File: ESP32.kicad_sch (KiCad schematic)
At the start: 24 parts, among them IC1 LY68L6400SLIT, Q3 MUN5211DW1, U10 ESP32-S2FH4, U11 W25Q128JVS, U8 CP2104, Y4 40MHz

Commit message: тестирование
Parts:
- removed F2, F3: BLM15BC241SN1D, Fuse:Fuse_0402_1005Metric, symbol Device:Fuse
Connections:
- net ESP_3V3: now also U10.1 (VDDA@0), U10.20 (VDD3P3_RTC), U10.27 (VDD3P3_RTC_IO), U10.3 (VDD3P3@0), U10.4 (VDD3P3@1), U10.45 (VDD3P3_CPU), U10.51 (VDDA@1), U10.54 (VDDA@2)
- no-connect marks 41 -> 43
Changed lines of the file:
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@@
 (kicad_sch (version 20211123) (generator eeschema)
   (paper "A3")
-  (junction (at 107.95 22.86) (diameter 0) (color 0 0 0 0)
+  (junction (at 223.52 52.07) (diameter 0) (color 0 0 0 0)
+  )
+  (junction (at 60.96 152.4) (diameter 0) (color 0 0 0 0)
+  )
+  (junction (at 39.37 62.23) (diameter 0) (color 0 0 0 0)
+  )
+  (junction (at 218.44 46.99) (diameter 0) (color 0 0 0 0)
+  )
+  (junction (at 97.79 203.2) (diameter 0) (color 0 0 0 0)
+  )
+  (junction (at 25.4 69.85) (diameter 0) (color 0 0 0 0)
+  )
+  (junction (at 102.87 34.29) (diameter 0) (color 0 0 0 0)
+  )
+  (junction (at 30.48 69.85) (diameter 0) (color 0 0 0 0)
+  )
+  (junction (at 223.52 96.52) (diameter 0) (color 0 0 0 0)
+  )
+  (junction (at 130.81 195.58) (diameter 0) (color 0 0 0 0)
+  )
+  (junction (at 127 30.48) (diameter 0) (color 0 0 0 0)
+  )
+  (junction (at 138.43 22.86) (diameter 0) (color 0 0 0 0)
+  )
+  (junction (at 127 22.86) (diameter 0) (color 0 0 0 0)
   )
   (junction (at 92.71 34.29) (diameter 0) (color 0 0 0 0)
   )
-  (junction (at 223.52 52.07) (diameter 0) (color 0 0 0 0)
-  )
-  (junction (at 60.96 152.4) (diameter 0) (color 0 0 0 0)
-  )
-  (junction (at 39.37 62.23) (diameter 0) (color 0 0 0 0)
-  )
-  (junction (at 218.44 46.99) (diameter 0) (color 0 0 0 0)
-  )
-  (junction (at 97.79 203.2) (diameter 0) (color 0 0 0 0)
-  )
-  (junction (at 87.63 34.29) (diameter 0) (color 0 0 0 0)
-  )
-  (junction (at 25.4 69.85) (diameter 0) (color 0 0 0 0)
-  )
-  (junction (at 102.87 34.29) (diameter 0) (color 0 0 0 0)
-  )
-  (junction (at 30.48 69.85) (diameter 0) (color 0 0 0 0)
-  )
-  (junction (at 223.52 96.52) (diameter 0) (color 0 0 0 0)
-  )
-  (junction (at 130.81 195.58) (diameter 0) (color 0 0 0 0)
-  )
-  (junction (at 127 30.48) (diameter 0) (color 0 0 0 0)
-  )
-  (junction (at 138.43 22.86) (diameter 0) (color 0 0 0 0)
-  )
-  (junction (at 127 22.86) (diameter 0) (color 0 0 0 0)
-  )
   (junction (at 97.79 34.29) (diameter 0) (color 0 0 0 0)
   )
@@
   (junction (at 149.86 22.86) (diameter 0) (color 0 0 0 0)
   )
+  (junction (at 105.41 34.29) (diameter 0) (color 0 0 0 0)
+  )
   (junction (at 138.43 30.48) (diameter 0) (color 0 0 0 0)
   )
@@
   )
   (junction (at 21.59 62.23) (diameter 0) (color 0 0 0 0)
+  )
+  (junction (at 90.17 34.29) (diameter 0) (color 0 0 0 0)
   )
   (junction (at 220.98 90.17) (diameter 0) (color 0 0 0 0)
@@
   (no_connect (at 73.66 172.72))
   (no_connect (at 73.66 175.26))
+  (no_connect (at 66.04 48.26))
+  (no_connect (at 66.04 45.72))
   (bus_entry (at 148.59 68.58) (size -2.54 2.54)
     (stroke (width 0) (type default) (color 0 0 0 0))
@@
     (stroke (width 0) (type default) (color 0 0 0 0))
   )
+  (wire (pts (xy 105.41 22.86) (xy 105.41 34.29))
+    (stroke (width 0) (type default) (color 0 0 0 0))
+  )
   (polyline (pts (xy 199.39 12.7) (xy 199.39 130.81))
     (stroke (width 0) (type default) (color 0 0 0 0))
@@
     (stroke (width 0) (type default) (color 0 0 0 0))
   )
-  (wire (pts (xy 93.98 30.48) (xy 92.71 30.48))
-    (stroke (width 0) (type default) (color 0 0 0 0))
-  )
   (wire (pts (xy 138.43 22.86) (xy 127 22.86))
     (stroke (width 0) (type default) (color 0 0 0 0))
@@
     (stroke (width 0) (type default) (color 0 0 0 0))
   )
-  (wire (pts (xy 101.6 30.48) (xy 107.95 30.48))
-    (stroke (width 0) (type default) (color 0 0 0 0))
-  )
   (wire (pts (xy 46.99 152.4) (xy 58.42 152.4))
     (stroke (width 0) (type default) (color 0 0 0 0))
@@
     (stroke (width 0) (type default) (color 0 0 0 0))
   )
+  (wire (pts (xy 90.17 34.29) (xy 92.71 34.29))
+    (stroke (width 0) (type default) (color 0 0 0 0))
+  )
   (polyline (pts (xy 12.7 132.08) (xy 147.32 132.08))
     (stroke (width 0) (type default) (color 0 0 0 0))
@@
     (stroke (width 0) (type default) (color 0 0 0 0))
   )
-  (wire (pts (xy 107.95 22.86) (xy 101.6 22.86))
-    (stroke (width 0) (type default) (color 0 0 0 0))
-  )
   (wire (pts (xy 130.81 195.58) (xy 130.81 194.31))
     (stroke (width 0) (type default) (color 0 0 0 0))
@@
     (stroke (width 0) (type default) (color 0 0 0 0))
   )
-  (wire (pts (xy 115.57 22.86) (xy 107.95 22.86))
-    (stroke (width 0) (type default) (color 0 0 0 0))
-  )
   (wire (pts (xy 163.83 46.99) (xy 165.1 46.99))
     (stroke (width 0) (type default) (color 0 0 0 0))
@@
     (stroke (width 0) (type default) (color 0 0 0 0))
   )
-  (wire (pts (xy 92.71 34.29) (xy 92.71 30.48))
-    (stroke (width 0) (type default) (color 0 0 0 0))
-  )
   (wire (pts (xy 130.81 185.42) (xy 130.81 186.69))
     (stroke (width 0) (type default) (color 0 0 0 0))
@@
     (stroke (width 0) (type default) (color 0 0 0 0))
   )
-  (wire (pts (xy 87.63 22.86) (xy 93.98 22.86))
-    (stroke (width 0) (type default) (color 0 0 0 0))
-  )
   (polyline (pts (xy 147.32 229.87) (xy 12.7 229.87))
     (stroke (width 0) (type default) (color 0 0 0 0))
@@
     (stroke (width 0) (type default) (color 0 0 0 0))
   )
-  (wire (pts (xy 87.63 34.29) (xy 87.63 22.86))
-    (stroke (width 0) (type default) (color 0 0 0 0))
-  )
   (wire (pts (xy 115.57 30.48) (xy 127 30.48))
     (stroke (width 0) (type default) (color 0 0 0 0))
@@
     (stroke (width 0) (type default) (color 0 0 0 0))
   )
-  (wire (pts (xy 107.95 30.48) (xy 107.95 22.86))
-    (stroke (width 0) (type default) (color 0 0 0 0))
-  )
   (wire (pts (xy 110.49 195.58) (xy 130.81 195.58))
     (stroke (width 0) (type default) (color 0 0 0 0))
@@
   )
   (wire (pts (xy 110.49 214.63) (xy 110.49 212.09))
+    (stroke (width 0) (type default) (color 0 0 0 0))
+  )
+  (wire (pts (xy 105.41 22.86) (xy 115.57 22.86))
     (stroke (width 0) (type default) (color 0 0 0 0))
   )
@@
     (pin "2")
   )
-  (symbol (lib_id "Device:Fuse") (at 97.79 22.86 270) (unit 1)
-    (in_bom yes) (on_board yes)
-    (property "Reference" "F2" (id 0) (at 97.79 17.8562 90))
-    (property "Value" "BLM15BC241SN1D" (id 1) (at 97.79 20.32 90))
-    (property "Footprint" "Fuse:Fuse_0402_1005Metric" (id 2) (at 97.79 21.082 90)
-      (effects (font (size 1.27 1.27)) hide)
-    )
-    (property "Datasheet" "~" (id 3) (at 97.79 22.86 0)
-      (effects (font (size 1.27 1.27)) hide)
-    )
-    (property "Manufacturer_Part_Number" "BLM15BC241SN1D" (id 8) (at 97.79 22.86 0)
-      (effects (font (size 1.27 1.27)) hide)
-    )
-    (pin "1")
-    (pin "2")
-  )
   (symbol (lib_id "Device:C") (at 115.57 26.67 0) (unit 1)
     (in_bom yes) (on_board yes)
@@
       (effects (font (size 1.27 1.27)) hide)
     )
-    (pin "1")
-    (pin "2")
-  )
-  (symbol (lib_id "Device:Fuse") (at 97.79 30.48 270) (unit 1)
-    (in_bom yes) (on_board yes)
-    (property "Reference" "F3" (id 0) (at 97.79 25.4762 90))
-    (property "Value" "BLM15BC241SN1D" (id 1) (at 97.79 27.94 90))
-    (property "Footprint" "Fuse:Fuse_0402_1005Metric" (id 2) (at 97.79 28.702 90)
-      (effects (font (size 1.27 1.27)) hide)
-    )
-    (property "Datasheet" "~" (id 3) (at 97.79 30.48 0)
-      (effects (font (size 1.27 1.27)) hide)
-    )
-    (property "Manufacturer_Part_Number" "BLM15BC241SN1D" (id 8) (at 97.79 30.48 0)
-      (effects (font (size 1.27 1.27)) hide)
-    )

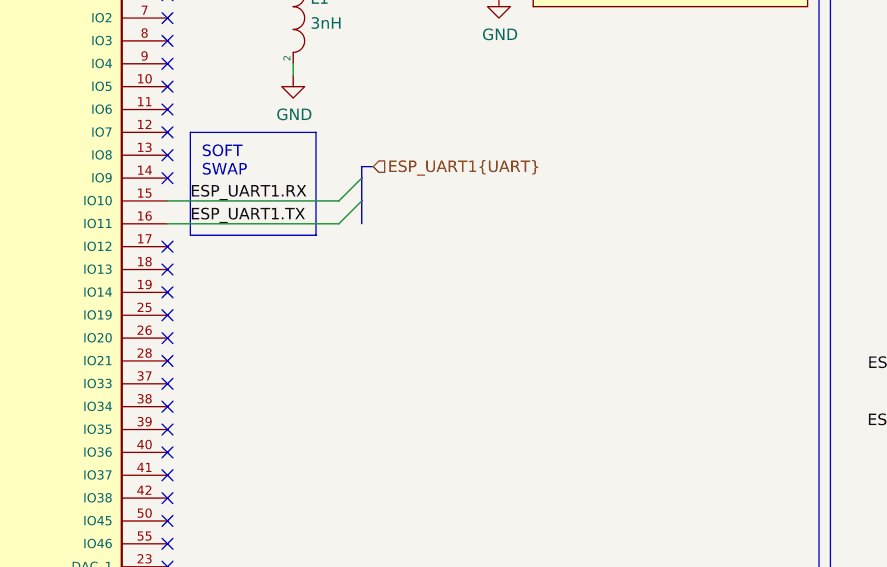
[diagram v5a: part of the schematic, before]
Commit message: Adding esp32 gpio pins
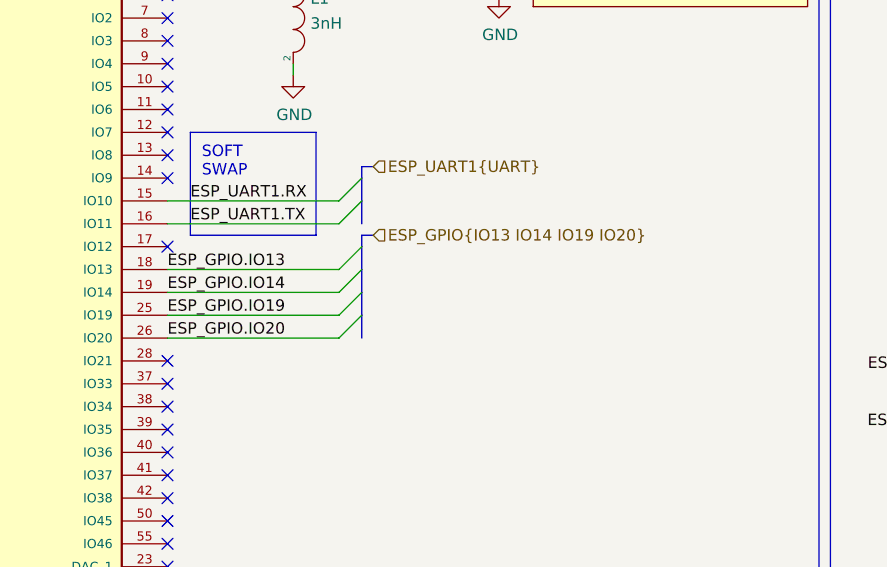
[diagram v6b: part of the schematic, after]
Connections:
- net ESP_GPIO.IO13: now reaches U10.18 (IO13)
- net ESP_GPIO.IO14: now reaches U10.19 (IO14)
- net ESP_GPIO.IO19: now reaches U10.25 (IO19)
- net ESP_GPIO.IO20: now reaches U10.26 (IO20)
- no-connect marks 43 -> 39
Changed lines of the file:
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@@
   (no_connect (at 127 55.88))
   (no_connect (at 127 58.42))
-  (no_connect (at 127 86.36))
-  (no_connect (at 127 83.82))
-  (no_connect (at 127 81.28))
-  (no_connect (at 127 78.74))
   (no_connect (at 127 76.2))
   (no_connect (at 127 66.04))
@@
   (no_connect (at 66.04 48.26))
   (no_connect (at 66.04 45.72))
+  (bus_entry (at 148.59 76.2) (size -2.54 2.54)
+    (stroke (width 0) (type default) (color 0 0 0 0))
+  )
+  (bus_entry (at 148.59 78.74) (size -2.54 2.54)
+    (stroke (width 0) (type default) (color 0 0 0 0))
+  )
   (bus_entry (at 148.59 68.58) (size -2.54 2.54)
     (stroke (width 0) (type default) (color 0 0 0 0))
@@
     (stroke (width 0) (type default) (color 0 0 0 0))
   )
+  (bus_entry (at 148.59 83.82) (size -2.54 2.54)
+    (stroke (width 0) (type default) (color 0 0 0 0))
+  )
   (bus_entry (at 31.75 170.18) (size 2.54 2.54)
     (stroke (width 0) (type default) (color 0 0 0 0))
@@
     (stroke (width 0) (type default) (color 0 0 0 0))
   )
+  (bus_entry (at 148.59 81.28) (size -2.54 2.54)
+    (stroke (width 0) (type default) (color 0 0 0 0))
+  )
   (bus (pts (xy 148.59 71.12) (xy 148.59 68.58))
     (stroke (width 0) (type default) (color 0 0 0 0))
@@
     (stroke (width 0) (type default) (color 0 0 0 0))
   )
+  (bus (pts (xy 148.59 76.2) (xy 148.59 74.93))
+    (stroke (width 0) (type default) (color 0 0 0 0))
+  )
   (wire (pts (xy 138.43 22.86) (xy 127 22.86))
     (stroke (width 0) (type default) (color 0 0 0 0))
@@
     (stroke (width 0) (type default) (color 0 0 0 0))
   )
+  (bus (pts (xy 148.59 76.2) (xy 148.59 78.74))
+    (stroke (width 0) (type default) (color 0 0 0 0))
+  )
   (wire (pts (xy 63.5 66.04) (xy 66.04 66.04))
     (stroke (width 0) (type default) (color 0 0 0 0))
@@
     (stroke (width 0) (type default) (color 0 0 0 0))
   )
+  (wire (pts (xy 127 83.82) (xy 146.05 83.82))
+    (stroke (width 0) (type default) (color 0 0 0 0))
+  )
   (wire (pts (xy 110.49 208.28) (xy 110.49 210.82))
     (stroke (width 0) (type default) (color 0 0 0 0))
@@
     (stroke (width 0) (type default) (color 0 0 0 0))
   )
+  (wire (pts (xy 127 81.28) (xy 146.05 81.28))
+    (stroke (width 0) (type default) (color 0 0 0 0))
+  )
   (wire (pts (xy 99.06 210.82) (xy 99.06 219.71))
     (stroke (width 0) (type default) (color 0 0 0 0))
@@
     (stroke (width 0) (type default) (color 0 0 0 0))
   )
+  (bus (pts (xy 148.59 74.93) (xy 149.86 74.93))
+    (stroke (width 0) (type default) (color 0 0 0 0))
+  )
   (wire (pts (xy 130.81 185.42) (xy 130.81 186.69))
     (stroke (width 0) (type default) (color 0 0 0 0))
@@
     (stroke (width 0) (type default) (color 0 0 0 0))
   )
+  (bus (pts (xy 148.59 78.74) (xy 148.59 81.28))
+    (stroke (width 0) (type default) (color 0 0 0 0))
+  )
   (wire (pts (xy 127 71.12) (xy 146.05 71.12))
     (stroke (width 0) (type default) (color 0 0 0 0))
@@
     (stroke (width 0) (type default) (color 0 0 0 0))
   )
+  (bus (pts (xy 148.59 83.82) (xy 148.59 86.36))
+    (stroke (width 0) (type default) (color 0 0 0 0))
+  )
   (wire (pts (xy 127 30.48) (xy 138.43 30.48))
     (stroke (width 0) (type default) (color 0 0 0 0))
@@
     (stroke (width 0) (type default) (color 0 0 0 0))
   )
+  (wire (pts (xy 127 86.36) (xy 146.05 86.36))
+    (stroke (width 0) (type default) (color 0 0 0 0))
+  )
   (wire (pts (xy 257.81 44.45) (xy 252.73 44.45))
     (stroke (width 0) (type default) (color 0 0 0 0))
@@
     (stroke (width 0) (type default) (color 0 0 0 0))
   )
+  (bus (pts (xy 148.59 81.28) (xy 148.59 83.82))
+    (stroke (width 0) (type default) (color 0 0 0 0))
+  )
   (wire (pts (xy 115.57 30.48) (xy 127 30.48))
     (stroke (width 0) (type default) (color 0 0 0 0))
@@
   )
   (wire (pts (xy 130.81 196.85) (xy 130.81 195.58))
+    (stroke (width 0) (type default) (color 0 0 0 0))
+  )
+  (wire (pts (xy 127 78.74) (xy 146.05 78.74))
     (stroke (width 0) (type default) (color 0 0 0 0))
   )
@@
     (effects (font (size 1.27 1.27)) (justify left bottom))
   )
+  (label "ESP_GPIO.IO14" (at 127 81.28 0)
+    (effects (font (size 1.27 1.27)) (justify left bottom))
+  )
   (label "ESP_NRST" (at 116.84 195.58 0)
     (effects (font (size 1.27 1.27)) (justify left bottom))
   )
+  (label "ESP_GPIO.IO19" (at 127 83.82 0)
+    (effects (font (size 1.27 1.27)) (justify left bottom))
+  )
   (label "ESP_SPI_HLD" (at 257.81 99.06 0)
     (effects (font (size 1.27 1.27)) (justify left bottom))
@@
     (effects (font (size 1.27 1.27)) (justify left bottom))
   )
+  (label "ESP_GPIO.IO20" (at 127 86.36 0)
+    (effects (font (size 1.27 1.27)) (justify left bottom))
+  )
   (label "ESP_SPI_3V3" (at 257.81 38.1 0)
     (effects (font (size 1.27 1.27)) (justify left bottom))
@@
     (effects (font (size 1.27 1.27)) (justify right bottom))
   )
+  (label "ESP_GPIO.IO13" (at 127 78.74 0)
+    (effects (font (size 1.27 1.27)) (justify left bottom))
+  )
   (label "ESP_SPI_CS1" (at 63.5 60.96 180)
     (effects (font (size 1.27 1.27)) (justify right bottom))
@@
     (effects (font (size 1.27 1.27)) (justify right bottom))
   )
+  (hierarchical_label "ESP_GPIO{IO13 IO14 IO19 IO20}" (shape input) (at 149.86 74.93 0)
+    (effects (font (size 1.27 1.27)) (justify left))
+  )
   (hierarchical_label "ESP_UART1{UART}" (shape input) (at 149.86 67.31 0)

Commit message: Little fix
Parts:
- C19, C32, C33, C34: Manufacturer_Part_Number (none) -> CL05B104KB54PNC
- C30, C31: Manufacturer_Part_Number (none) -> 0402CG150J500NT
- R14, R42: Manufacturer_Part_Number (none) -> 0402WGF1001TCE
- R15, R16, R17, R18: Manufacturer_Part_Number (none) -> 0402WGF1002TCE
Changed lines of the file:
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@@
+      (effects (font (size 1.27 1.27)) hide)
+    )
+    (property "Manufacturer_Part_Number" "0402WGF1002TCE" (id 4) (at 220.98 54.61 0)
       (effects (font (size 1.27 1.27)) hide)
     )
@@
       (effects (font (size 1.27 1.27)) hide)
     )
+    (property "Manufacturer_Part_Number" "0402WGF1002TCE" (id 4) (at 223.52 38.1 0)
+      (effects (font (size 1.27 1.27)) hide)
+    )
     (pin "1")
     (pin "2")
@@
       (effects (font (size 1.27 1.27)) hide)
     )
+    (property "Manufacturer_Part_Number" "0402WGF1002TCE" (id 4) (at 218.44 38.1 0)
+      (effects (font (size 1.27 1.27)) hide)
+    )
     (pin "1")
     (pin "2")
@@
       (effects (font (size 1.27 1.27)) hide)
     )
+    (property "Manufacturer_Part_Number" "CL05B104KB54PNC" (id 4) (at 115.57 26.67 0)
+      (effects (font (size 1.27 1.27)) hide)
+    )
     (pin "1")
     (pin "2")
@@
       (effects (font (size 1.27 1.27)) hide)
     )
+    (property "Manufacturer_Part_Number" "CL05B104KB54PNC" (id 4) (at 127 26.67 0)
+      (effects (font (size 1.27 1.27)) hide)
+    )
     (pin "1")
     (pin "2")
@@
     )
     (property "Datasheet" "~" (id 3) (at 138.43 26.67 0)
+      (effects (font (size 1.27 1.27)) hide)
+    )
+    (property "Manufacturer_Part_Number" "CL05B104KB54PNC" (id 4) (at 138.43 26.67 0)
       (effects (font (size 1.27 1.27)) hide)
     )
@@
       (effects (font (size 1.27 1.27)) hide)
     )
+    (property "Manufacturer_Part_Number" "0402WGF1002TCE" (id 4) (at 130.81 190.5 0)
+      (effects (font (size 1.27 1.27)) hide)
+    )
     (pin "1")
     (pin "2")
@@
       (effects (font (size 1.27 1.27)) hide)
     )
+    (property "Manufacturer_Part_Number" "0402CG150J500NT" (id 4) (at 21.59 66.04 0)
+      (effects (font (size 1.27 1.27)) hide)
+    )
     (pin "1")
     (pin "2")
@@
     )
     (property "Datasheet" "~" (id 3) (at 39.37 66.04 0)
+      (effects (font (size 1.27 1.27)) hide)
+    )
+    (property "Manufacturer_Part_Number" "0402CG150J500NT" (id 4) (at 39.37 66.04 0)
       (effects (font (size 1.27 1.27)) hide)
     )
@@
       (effects (font (size 1.27 1.27)) hide)
     )
+    (property "Manufacturer_Part_Number" "0402WGF1001TCE" (id 4) (at 58.42 93.98 0)
+      (effects (font (size 1.27 1.27)) hide)
+    )
     (pin "1")
     (pin "2")
@@
       (effects (font (size 1.27 1.27)) hide)
     )
+    (property "Manufacturer_Part_Number" "CL05B104KB54PNC" (id 4) (at 130.81 200.66 0)
+      (effects (font (size 1.27 1.27)) hide)
+    )
     (pin "1")
     (pin "2")
@@
       (effects (font (size 1.27 1.27)) hide)
     )
+    (property "Manufacturer_Part_Number" "0402WGF1001TCE" (id 4) (at 58.42 91.44 0)
+      (effects (font (size 1.27 1.27)) hide)
+    )

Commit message: First order
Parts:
- removed L1: 3nH, Inductor_SMD:L_0402_1005Metric, symbol pspice:INDUCTOR
- added C29: 1pF, Capacitor_SMD:C_0402_1005Metric, symbol Device:C
- C19, C32, C33, C34: Manufacturer_Part_Number CL05B104KB54PNC -> C1005X7R1H104KT000S
- C30, C31: Manufacturer_Part_Number 0402CG150J500NT -> GJM1555C1H150GB01D
- C38: Manufacturer_Part_Number CL31A226KAHNNNE -> CL05A106MP8NUB8
- L2: value 2nH -> 1nH
- R14, R42: Manufacturer_Part_Number 0402WGF1001TCE -> RN731ETTP1001B25
- R15, R16, R17, R18: Manufacturer_Part_Number 0402WGF1002TCE -> RNCF0402BTE10K0
- U11: Manufacturer_Part_Number W25Q128JVS -> W25Q128JVSIQ
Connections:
- net GND: now also C29.1
- net at ANT1.4 (FEEDING), L2.2: now also C29.2
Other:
- moved on the sheet: L2
